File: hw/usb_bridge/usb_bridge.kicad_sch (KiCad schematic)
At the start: 60 parts, among them J1 USB_C_Receptacle_USB2.0_14P, J2 DE9, U1 CH340E, U2 MAX485E, U3 CH334R, U5 MCP1754S-3302xCB, U6 TJA1051T-3, U8 74HC04, Y1 HCI XC53G2-12.000-F20LJDT

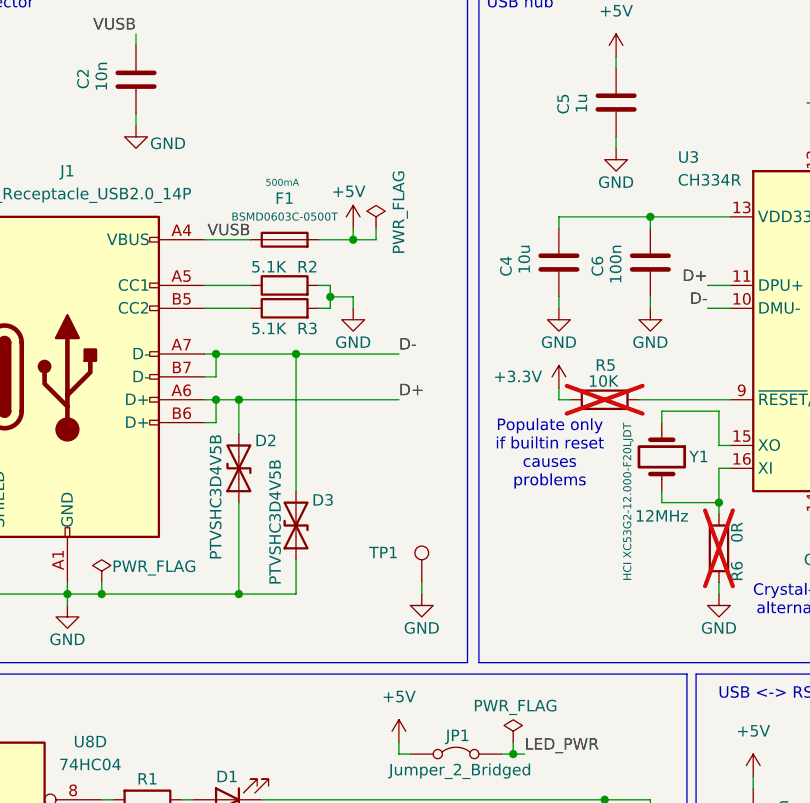
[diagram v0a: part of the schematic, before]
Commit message: Add 5V TP, Cleanup
Signed-off-by: Mateusz Pająk <22417805+Tai-Min@users.noreply.github.com>
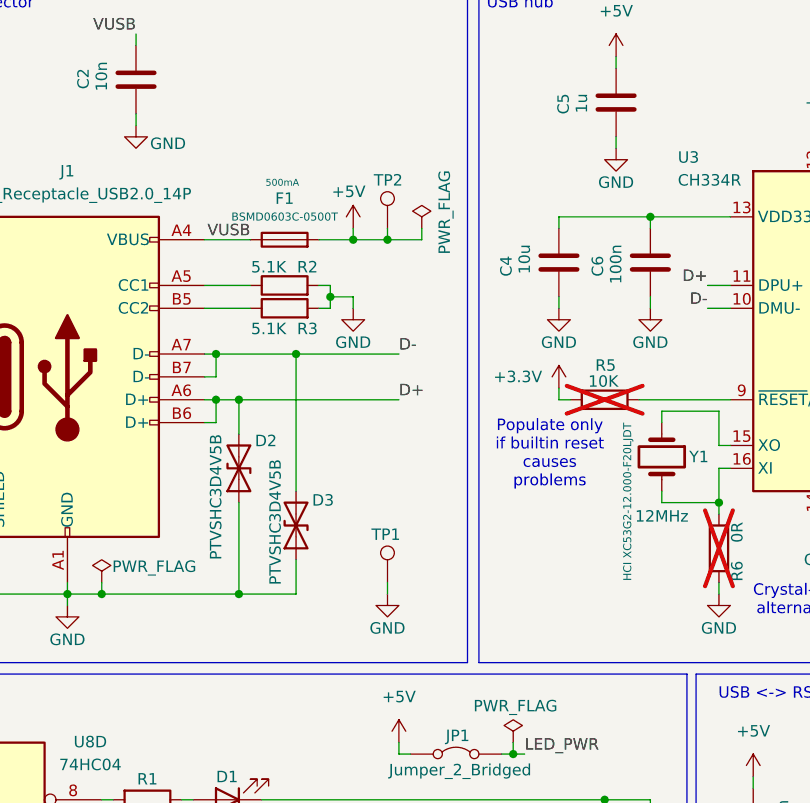
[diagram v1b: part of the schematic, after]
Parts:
- added TP2: TestPoint, TestPoint:TestPoint_Pad_D1.5mm, symbol Connector:TestPoint
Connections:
- net +5V: now also TP2.1
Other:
- moved on the sheet: TP1
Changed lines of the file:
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@@
 	)
 	(junction
+		(at 82.55 41.91)
+		(diameter 0)
+		(color 0 0 0 0)
+	)
+	(junction
 		(at 66.04 81.28)
 		(diameter 0)
@@
 	(wire
 		(pts
+			(xy 82.55 41.91) (xy 82.55 40.64)
+		)
+		(stroke
+			(width 0)
+			(type default)
+		)
+	)
+	(wire
+		(pts
 			(xy 63.5 54.61) (xy 63.5 57.15)
 		)
@@
 	(wire
 		(pts
+			(xy 86.36 40.64) (xy 86.36 41.91)
+		)
+		(stroke
+			(width 0)
+			(type default)
+		)
+	)
+	(wire
+		(pts
 			(xy 130.81 72.39) (xy 130.81 73.66)
 		)
@@
 	(wire
 		(pts
-			(xy 78.74 41.91) (xy 81.28 41.91)
+			(xy 78.74 41.91) (xy 82.55 41.91)
 		)
 		(stroke
@@
 	(wire
 		(pts
-			(xy 143.51 38.1) (xy 143.51 39.37)
+			(xy 86.36 41.91) (xy 82.55 41.91)
 		)
 		(stroke
@@
 	(wire
 		(pts
-			(xy 111.76 39.37) (xy 111.76 40.64)
+			(xy 143.51 38.1) (xy 143.51 39.37)
 		)
 		(stroke
@@
 	(wire
 		(pts
-			(xy 140.97 64.77) (xy 143.51 64.77)
+			(xy 111.76 39.37) (xy 111.76 40.64)
 		)
 		(stroke
@@
 	(wire
 		(pts
-			(xy 59.69 104.14) (xy 60.96 104.14)
+			(xy 140.97 64.77) (xy 143.51 64.77)
 		)
 		(stroke
@@
 	(wire
 		(pts
-			(xy 171.45 35.56) (xy 171.45 36.83)
+			(xy 59.69 104.14) (xy 60.96 104.14)
 		)
 		(stroke
@@
 	(wire
 		(pts
-			(xy 203.2 67.31) (xy 217.17 67.31)
+			(xy 171.45 35.56) (xy 171.45 36.83)
 		)
 		(stroke
@@
 	(wire
 		(pts
-			(xy 63.5 59.69) (xy 66.04 59.69)
+			(xy 203.2 67.31) (xy 217.17 67.31)
 		)
 		(stroke
@@
 	(wire
 		(pts
-			(xy 81.28 40.64) (xy 81.28 41.91)
+			(xy 63.5 59.69) (xy 66.04 59.69)
 		)
 		(stroke
@@
 	(wire
 		(pts
-			(xy 86.36 80.01) (xy 86.36 81.28)
+			(xy 82.55 80.01) (xy 82.55 81.28)
 		)
 		(stroke
@@
 	(symbol
 		(lib_id "Connector:TestPoint")
-		(at 86.36 80.01 0)
+		(at 82.55 80.01 0)
 		(unit 1)
 		(exclude_from_sim no)
@@
 		(dnp no)
 		(property "Reference" "TP1"
-			(at 80.518 76.708 0)
+			(at 80.772 74.676 0)
 			(effects
 				(font
@@
 		)
 		(property "Value" "TestPoint"
-			(at 88.9 77.9779 0)
+			(at 85.09 77.9779 0)
 			(effects
 				(font
@@
 		)
 		(property "Footprint" "TestPoint:TestPoint_Pad_D1.5mm"
-			(at 91.44 80.01 0)
+			(at 87.63 80.01 0)
 			(effects
 				(font
@@
 		)
 		(property "Datasheet" "~"
-			(at 91.44 80.01 0)
+			(at 87.63 80.01 0)
 			(effects
 				(font
@@
 		)
 		(property "Description" "test point"
-			(at 86.36 80.01 0)
+			(at 82.55 80.01 0)
 			(effects
 				(font
@@
 		)
 		(property "LCSC Part #" ""
-			(at 86.36 80.01 0)
+			(at 82.55 80.01 0)
 			(effects
 				(font
@@
 	)
 	(symbol
+		(lib_id "Connector:TestPoint")
+		(at 82.55 40.64 0)
+		(unit 1)
+		(exclude_from_sim no)
+		(in_bom yes)
+		(on_board yes)
+		(dnp no)
+		(property "Reference" "TP2"
+			(at 81.026 35.306 0)
+			(effects
+				(font
+					(size 1.27 1.27)
+				)
+				(justify left)
+			)
+		)
+		(property "Value" "TestPoint"
+			(at 85.09 38.6079 0)
+			(effects
+				(font
+					(size 1.27 1.27)
+				)
+				(justify left)
+				(hide yes)
+			)
+		)
+		(property "Footprint" "TestPoint:TestPoint_Pad_D1.5mm"
+			(at 87.63 40.64 0)
+			(effects
+				(font
+					(size 1.27 1.27)
+				)
+				(hide yes)
+			)
+		)
+		(property "Datasheet" "~"
+			(at 87.63 40.64 0)
+			(effects
+				(font
+					(size 1.27 1.27)
+				)
+				(hide yes)
+			)
+		)
+		(property "Description" "test point"
+			(at 82.55 40.64 0)
+			(effects
+				(font
+					(size 1.27 1.27)
+				)
+				(hide yes)
+			)
+		)
+		(property "LCSC Part #" ""
+			(at 82.55 40.64 0)
+			(effects
+				(font
+					(size 1.27 1.27)
+				)
+				(hide yes)
+			)
+		)
+		(pin "1"
+		)
+		(instances
+			(project "usb_bridge"
+				(path "/3b0cc3d4-df75-4145-abb6-d19d57c31f1b"
+					(reference "TP2")
+					(unit 1)
+				)
+			)
+		)
+	)
+	(symbol
 		(lib_id "74xx_IEEE:7404")
 		(at 80.01 151.13 0)
@@
 	(symbol
 		(lib_id "power:GND")
-		(at 86.36 81.28 0)
+		(at 82.55 81.28 0)
 		(unit 1)
 		(exclude_from_sim no)
@@
 		(dnp no)
 		(property "Reference" "#PWR011"
-			(at 86.36 87.63 0)
+			(at 82.55 87.63 0)
 			(effects
 				(font
@@
 		)
 		(property "Value" "GND"
-			(at 86.36 85.09 0)
+			(at 82.55 85.09 0)
 			(effects
 				(font
@@
 		)
 		(property "Footprint" ""
-			(at 86.36 81.28 0)
+			(at 82.55 81.28 0)
 			(effects
 				(font
@@
 		)
 		(property "Datasheet" ""
-			(at 86.36 81.28 0)
+			(at 82.55 81.28 0)
 			(effects
 				(font
@@
 		)
 		(property "Description" "Power symbol creates a global label with name \"GND\" , ground"
-			(at 86.36 81.28 0)
+			(at 82.55 81.28 0)
 			(effects
 				(font
@@
 	(symbol
 		(lib_id "power:PWR_FLAG")
-		(at 81.28 40.64 0)
+		(at 86.36 40.64 0)
 		(unit 1)
 		(exclude_from_sim no)
@@
 		(dnp no)
 		(property "Reference" "#FLG02"
-			(at 81.28 38.735 0)
+			(at 86.36 38.735 0)
 			(effects
 				(font
@@
 		)
 		(property "Value" "PWR_FLAG"
-			(at 83.82 38.862 90)
+			(at 88.9 38.862 90)
 			(effects
 				(font
@@
 		)
 		(property "Footprint" ""
-			(at 81.28 40.64 0)
+			(at 86.36 40.64 0)
 			(effects
 				(font
@@
 		)
 		(property "Datasheet" "~"
-			(at 81.28 40.64 0)
+			(at 86.36 40.64 0)
 			(effects
 				(font
@@
 		)
 		(property "Description" "Special symbol for telling ERC where power comes from"
-			(at 81.28 40.64 0)
+			(at 86.36 40.64 0)
 			(effects
 				(font

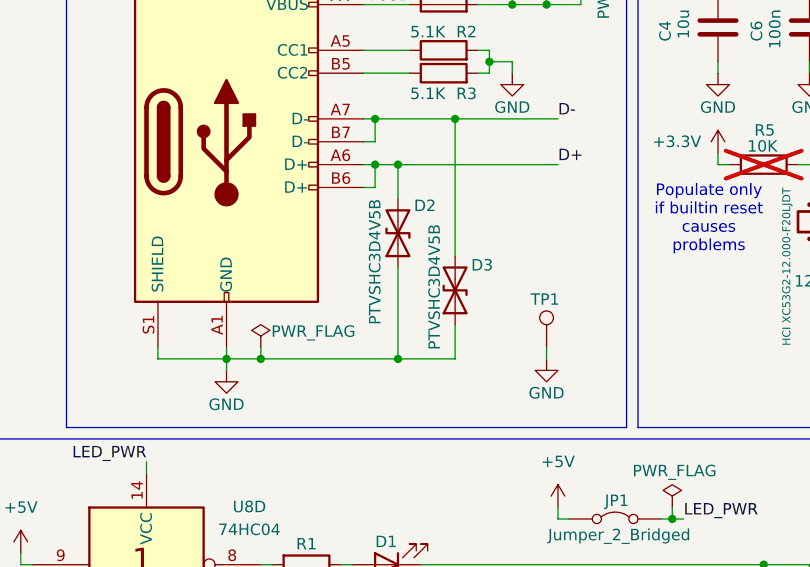
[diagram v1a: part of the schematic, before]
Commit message: Replace USB-C TVS with working ones, replace footprint of TVS to hand solder version
Signed-off-by: Mateusz Pajak <22417805+Tai-Min@users.noreply.github.com>
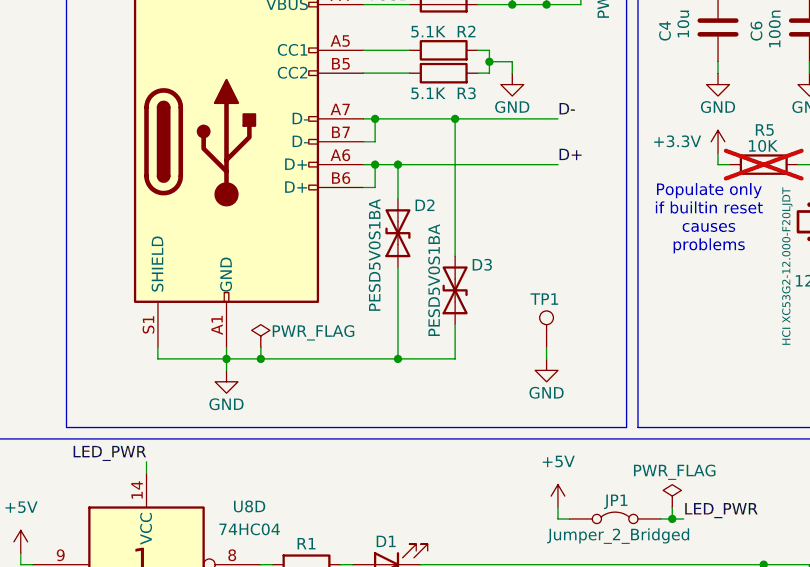
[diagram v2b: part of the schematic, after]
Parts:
- D2, D3: value PTVSHC3D4V5B -> PESD5V0S1BA; footprint Diode_SMD:D_SOD-323 -> Diode_SMD:D_SOD-323_HandSoldering
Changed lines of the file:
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@@
 			)
 		)
-		(property "Value" "PTVSHC3D4V5B"
+		(property "Value" "PESD5V0S1BA"
 			(at 70.104 66.294 0)
 			(effects
@@
 			)
 		)
-		(property "Footprint" "Diode_SMD:D_SOD-323"
+		(property "Footprint" "Diode_SMD:D_SOD-323_HandSoldering"
 			(at 72.39 73.66 0)
 			(effects
@@
 			)
 		)
-		(property "Value" "PTVSHC3D4V5B"
+		(property "Value" "PESD5V0S1BA"
 			(at 63.5 63.5 0)
 			(effects
@@
 			)
 		)
-		(property "Footprint" "Diode_SMD:D_SOD-323"
+		(property "Footprint" "Diode_SMD:D_SOD-323_HandSoldering"
 			(at 66.04 67.31 0)
 			(effects
